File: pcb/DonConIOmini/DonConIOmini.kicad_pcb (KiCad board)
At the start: 2 copper layers, 54 x 64 mm, 96 parts, among them J1 Ka Left, J2 Don Left, J3 Don Right, J4 Ka Right, J5 Pad, U1 TL074, U2 TL074, U3 RP2040-Zero, U5 MCP3204, U6 MCP1541-TT, U7 TXB0104D

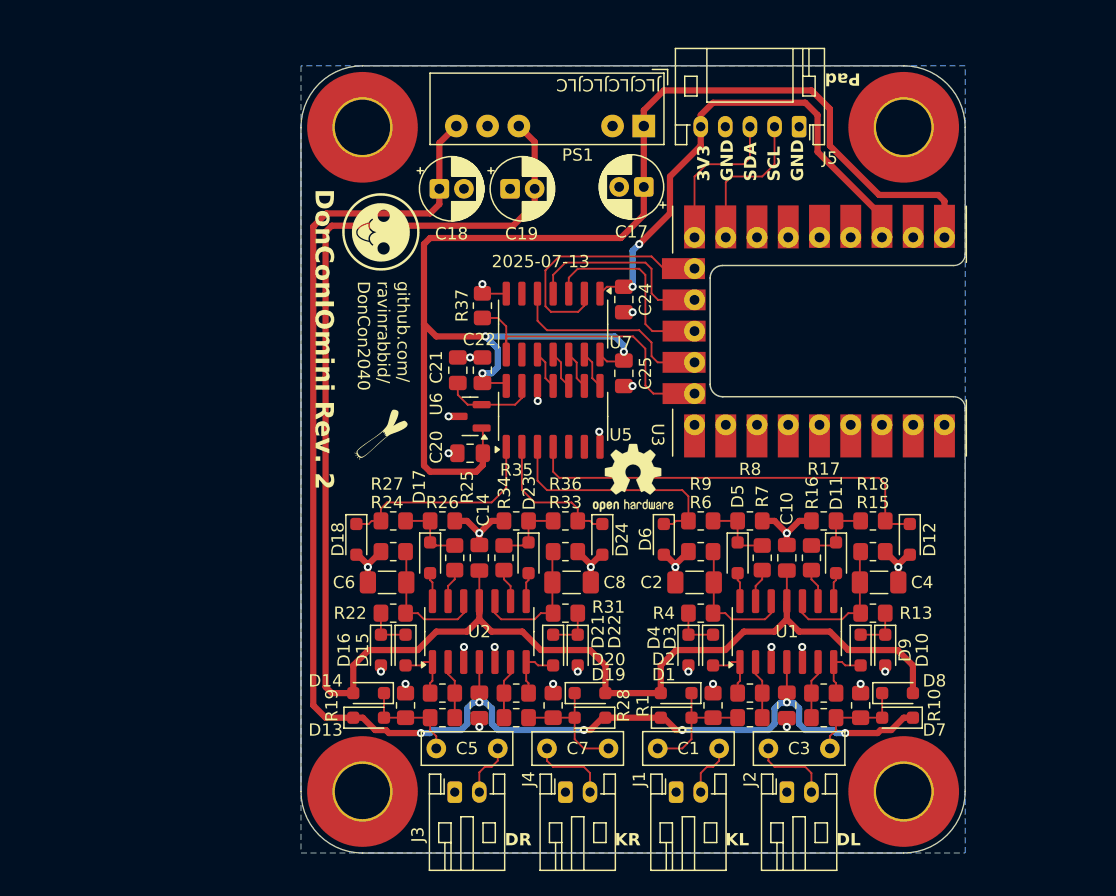
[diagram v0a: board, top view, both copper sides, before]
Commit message: Update DonConIOmini PCB to rev 2.1
Add SERVICE, COIN, and TEST signal connections on previously
unconnected GP0-GP2 pins. Add 1x04 connectors for the new signals.

Co-Authored-By: Claude Opus 4.6 <noreply@anthropic.com>
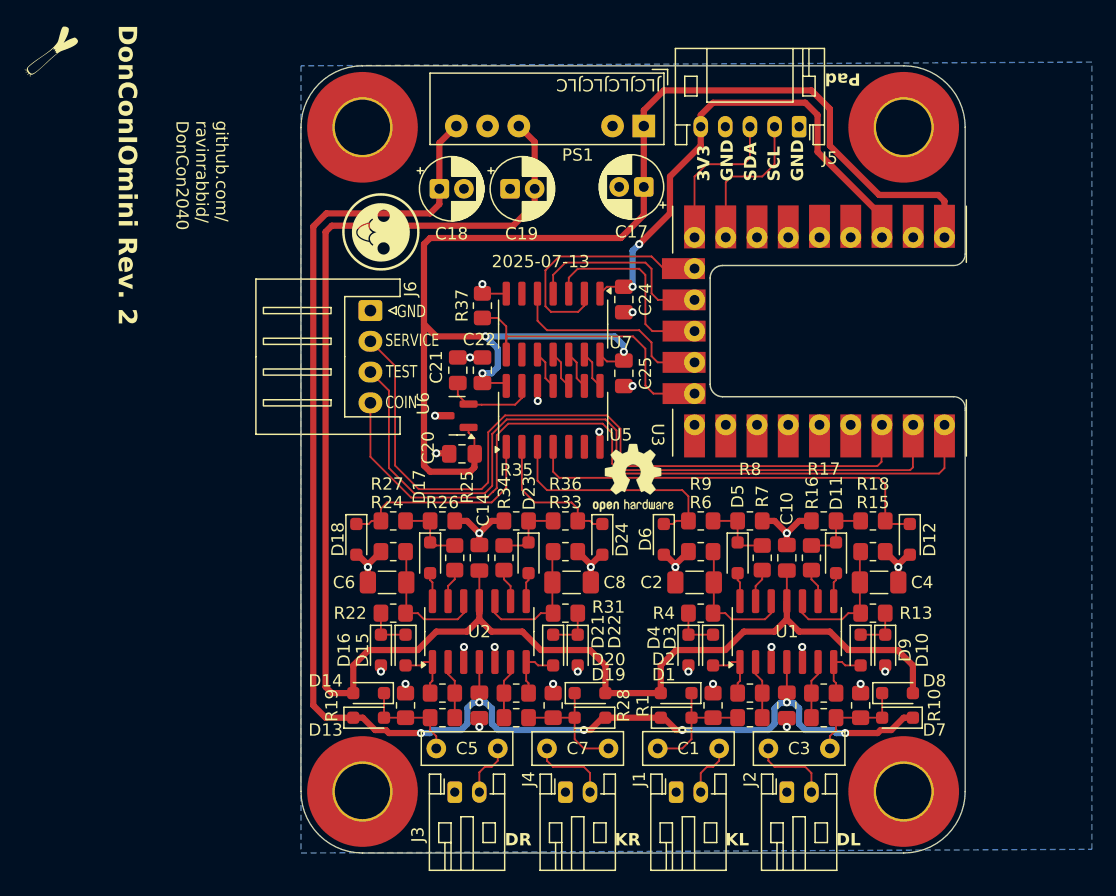
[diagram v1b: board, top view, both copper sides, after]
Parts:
- added J6: SERVICE, Connector_JST:JST_XH_S4B-XH-A_1x04_P2.50mm_Horizontal, F.Cu at (55.6, 71.9)
- moved REF** 41.1 mm to (29.7, 50.9)
- moved U6 1.06 mm to (62.7, 80.5)
- moved C20 0.66 mm to (63.1, 83.5)
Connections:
- U3 pad 10: unconnected-(U3-GP0-Pad10)_1 -> COIN
- U3 pad 11: unconnected-(U3-GP1-Pad11)_1 -> TEST
- U3 pad 12: unconnected-(U3-GP2-Pad12) -> SERVICE
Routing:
- net COIN: track 0.00 -> 63.4 mm
- net TEST: track 0.00 -> 62.6 mm
- net SERVICE: track 0.00 -> 61.5 mm
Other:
- board text added: "COIN"
- board text added: "SERVICE"
- board text added: "TEST"
